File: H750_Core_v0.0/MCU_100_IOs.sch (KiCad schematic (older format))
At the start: 32 parts, among them U1 750VB_3Parts, U2 RESET, U3 USER, Y1 NX2016SA 25MHz, Y2 NX3215SA 32.768KHz

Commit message: PCB layout finished
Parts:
- JP1, JP10, JP11, JP12, JP13, JP14, JP15, JP16, JP2, JP3, JP4, JP5, JP6, JP7, JP8, JP9: footprint Resistor_SMD:R_0603_1608Metric -> H750_Core:JP
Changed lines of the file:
@@
 F 0 "JP1" H 5650 5635 50  0000 C CNN
 F 1 "Jumper_2_Open" H 5650 5544 50  0000 C CNN
-F 2 "Resistor_SMD:R_0603_1608Metric" H 5650 5400 50  0001 C CNN
+F 2 "H750_Core:JP" H 5650 5400 50  0001 C CNN
 F 3 "~" H 5650 5400 50  0001 C CNN
 	1    5650 5400
@@
 F 0 "JP2" H 5650 5735 50  0000 C CNN
 F 1 "Jumper_2_Open" H 5650 5644 50  0000 C CNN
-F 2 "Resistor_SMD:R_0603_1608Metric" H 5650 5500 50  0001 C CNN
+F 2 "H750_Core:JP" H 5650 5500 50  0001 C CNN
 F 3 "~" H 5650 5500 50  0001 C CNN
 	1    5650 5500
@@
 F 0 "JP10" H 5850 4495 50  0000 C CNN
 F 1 "Jumper_2_Bridged" H 5850 4404 50  0000 C CNN
-F 2 "Resistor_SMD:R_0603_1608Metric" H 5850 4300 50  0001 C CNN
+F 2 "H750_Core:JP" H 5850 4300 50  0001 C CNN
 F 3 "~" H 5850 4300 50  0001 C CNN
 	1    5850 4300
@@
 F 0 "JP9" H 5850 4195 50  0000 C CNN
 F 1 "Jumper_2_Bridged" H 5850 4104 50  0000 C CNN
-F 2 "Resistor_SMD:R_0603_1608Metric" H 5850 4000 50  0001 C CNN
+F 2 "H750_Core:JP" H 5850 4000 50  0001 C CNN
 F 3 "~" H 5850 4000 50  0001 C CNN
 	1    5850 4000
@@
 F 0 "JP4" H 5850 2595 50  0000 C CNN
 F 1 "Jumper_2_Bridged" H 5850 2504 50  0000 C CNN
-F 2 "Resistor_SMD:R_0603_1608Metric" H 5850 2400 50  0001 C CNN
+F 2 "H750_Core:JP" H 5850 2400 50  0001 C CNN
 F 3 "~" H 5850 2400 50  0001 C CNN
 	1    5850 2400
@@
 F 0 "JP3" H 5850 2495 50  0000 C CNN
 F 1 "Jumper_2_Bridged" H 5850 2404 50  0000 C CNN
-F 2 "Resistor_SMD:R_0603_1608Metric" H 5850 2300 50  0001 C CNN
+F 2 "H750_Core:JP" H 5850 2300 50  0001 C CNN
 F 3 "~" H 5850 2300 50  0001 C CNN
 	1    5850 2300
@@
 F 0 "JP5" H 5850 3095 50  0000 C CNN
 F 1 "Jumper_2_Bridged" H 5850 3004 50  0000 C CNN
-F 2 "Resistor_SMD:R_0603_1608Metric" H 5850 2900 50  0001 C CNN
+F 2 "H750_Core:JP" H 5850 2900 50  0001 C CNN
 F 3 "~" H 5850 2900 50  0001 C CNN
 	1    5850 2900
@@
 F 0 "JP11" H 5850 4595 50  0000 C CNN
 F 1 "Jumper_2_Bridged" H 5850 4504 50  0000 C CNN
-F 2 "Resistor_SMD:R_0603_1608Metric" H 5850 4400 50  0001 C CNN
+F 2 "H750_Core:JP" H 5850 4400 50  0001 C CNN
 F 3 "~" H 5850 4400 50  0001 C CNN
 	1    5850 4400
@@
 F 0 "JP14" H 9700 3595 50  0000 C CNN
 F 1 "Jumper_2_Bridged" H 9700 3504 50  0000 C CNN
-F 2 "Resistor_SMD:R_0603_1608Metric" H 9700 3400 50  0001 C CNN
+F 2 "H750_Core:JP" H 9700 3400 50  0001 C CNN
 F 3 "~" H 9700 3400 50  0001 C CNN
 	1    9700 3400
@@
 F 0 "JP13" H 9700 3495 50  0000 C CNN
 F 1 "Jumper_2_Bridged" H 9700 3404 50  0000 C CNN
-F 2 "Resistor_SMD:R_0603_1608Metric" H 9700 3300 50  0001 C CNN
+F 2 "H750_Core:JP" H 9700 3300 50  0001 C CNN
 F 3 "~" H 9700 3300 50  0001 C CNN
 	1    9700 3300
@@
 F 0 "JP15" H 9700 3695 50  0000 C CNN
 F 1 "Jumper_2_Bridged" H 9700 3604 50  0000 C CNN
-F 2 "Resistor_SMD:R_0603_1608Metric" H 9700 3500 50  0001 C CNN
+F 2 "H750_Core:JP" H 9700 3500 50  0001 C CNN
 F 3 "~" H 9700 3500 50  0001 C CNN
 	1    9700 3500
@@
 F 0 "JP12" H 9700 2695 50  0000 C CNN
 F 1 "Jumper_2_Bridged" H 9700 2604 50  0000 C CNN
-F 2 "Resistor_SMD:R_0603_1608Metric" H 9700 2500 50  0001 C CNN
+F 2 "H750_Core:JP" H 9700 2500 50  0001 C CNN
 F 3 "~" H 9700 2500 50  0001 C CNN
 	1    9700 2500
@@
 F 0 "JP8" H 5850 3895 50  0000 C CNN
 F 1 "Jumper_2_Bridged" H 5850 3804 50  0000 C CNN
-F 2 "Resistor_SMD:R_0603_1608Metric" H 5850 3700 50  0001 C CNN
+F 2 "H750_Core:JP" H 5850 3700 50  0001 C CNN
 F 3 "~" H 5850 3700 50  0001 C CNN
 	1    5850 3700
@@
 F 0 "JP7" H 5850 3795 50  0000 C CNN
 F 1 "Jumper_2_Bridged" H 5850 3704 50  0000 C CNN
-F 2 "Resistor_SMD:R_0603_1608Metric" H 5850 3600 50  0001 C CNN
+F 2 "H750_Core:JP" H 5850 3600 50  0001 C CNN
 F 3 "~" H 5850 3600 50  0001 C CNN
 	1    5850 3600
@@
 F 0 "JP6" H 5850 3695 50  0000 C CNN
 F 1 "Jumper_2_Bridged" H 5850 3604 50  0000 C CNN
-F 2 "Resistor_SMD:R_0603_1608Metric" H 5850 3500 50  0001 C CNN
+F 2 "H750_Core:JP" H 5850 3500 50  0001 C CNN
 F 3 "~" H 5850 3500 50  0001 C CNN
 	1    5850 3500
@@
 F 0 "JP16" H 13050 7745 50  0000 C CNN
 F 1 "Jumper_2_Bridged" H 13050 7654 50  0000 C CNN
-F 2 "Resistor_SMD:R_0603_1608Metric" H 13050 7550 50  0001 C CNN
+F 2 "H750_Core:JP" H 13050 7550 50  0001 C CNN
 F 3 "~" H 13050 7550 50  0001 C CNN
 	1    13050 7550

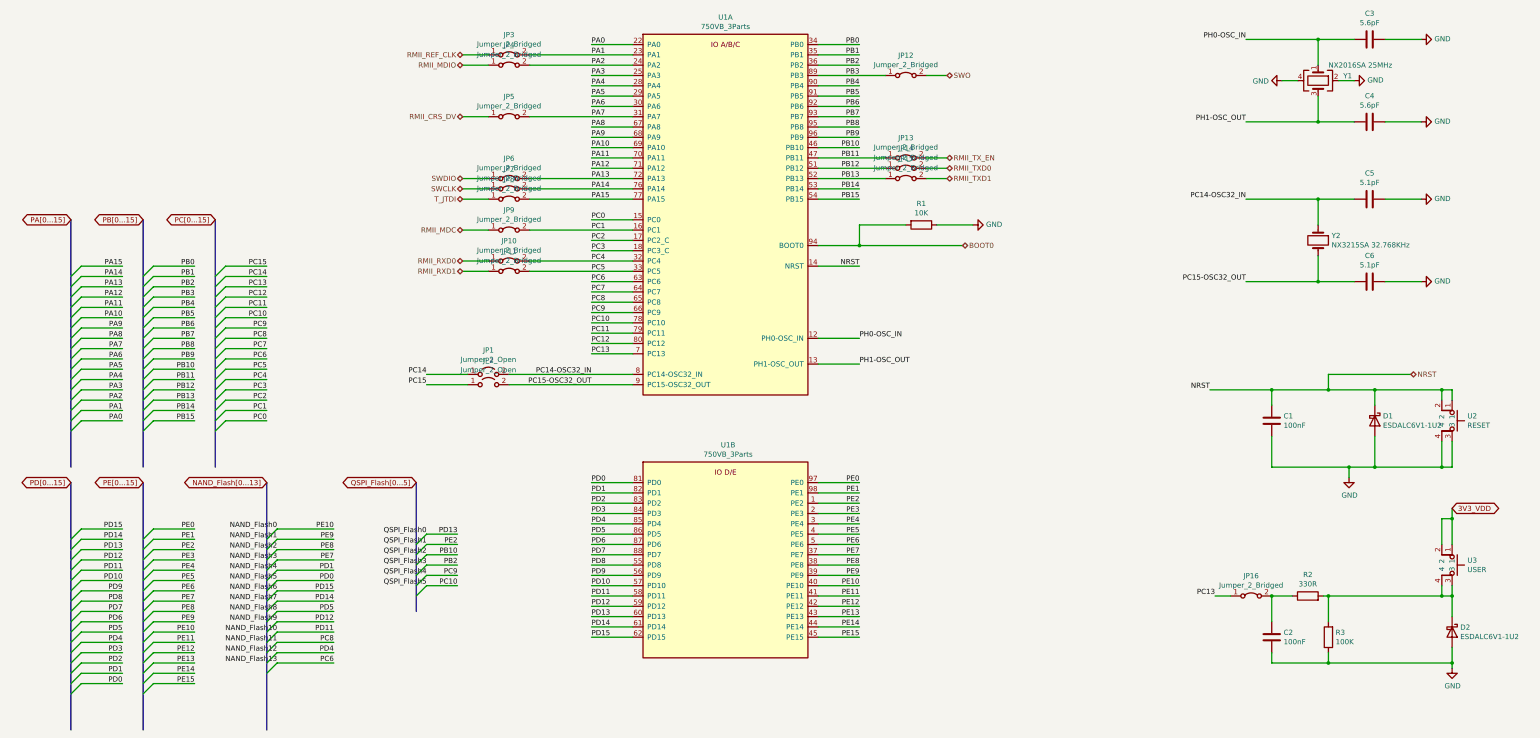
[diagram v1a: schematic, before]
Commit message: 修改编程接口
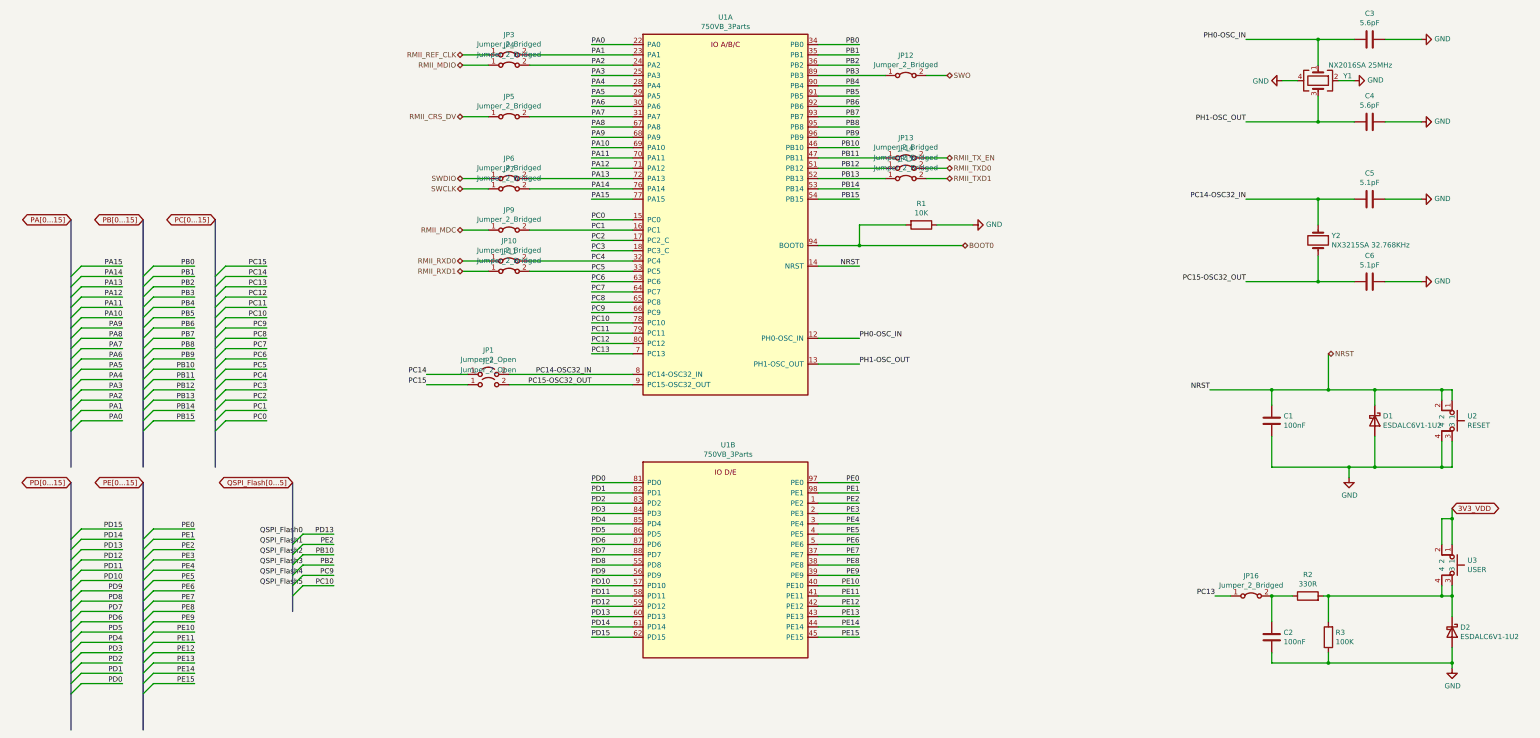
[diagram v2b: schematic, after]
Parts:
- removed JP8: Jumper_2_Bridged, H750_Core:JP, symbol Jumper:Jumper_2_Bridged
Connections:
- net NAND_Flash0 renamed PE10
- net NAND_Flash1 renamed PE9
- net NAND_Flash10 renamed PD11
- net NAND_Flash11 renamed PC8
- net NAND_Flash12 renamed PD4
- net NAND_Flash13 renamed PC6
- net NAND_Flash2 renamed PE8
- net NAND_Flash3 renamed PE7
- net NAND_Flash4 renamed PD1
- net NAND_Flash5 renamed PD0
- net NAND_Flash6 renamed PD15
- net NAND_Flash7 renamed PD14
- net NAND_Flash8 renamed PD5
- net NAND_Flash9 renamed PD12
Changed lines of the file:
@@
 EESchema Schematic File Version 4
-LIBS:H750_Core-cache
 EELAYER 30 0
 EELAYER END
@@
 Text HLabel 5400 3600 0    50   BiDi ~ 0
 SWCLK
-Text HLabel 5400 3700 0    50   BiDi ~ 0
-T_JTDI
 $Comp
 L Jumper:Jumper_2_Bridged JP12
@@
 	1    0    0    -1
 $EndComp
-$Comp
-L Jumper:Jumper_2_Bridged JP8
-U 1 1 5DA28DD9
-P 5850 3700
-F 0 "JP8" H 5850 3895 50  0000 C CNN
-F 1 "Jumper_2_Bridged" H 5850 3804 50  0000 C CNN
-F 2 "H750_Core:JP" H 5850 3700 50  0001 C CNN
-F 3 "~" H 5850 3700 50  0001 C CNN
-	1    5850 3700
-	1    0    0    -1
-$EndComp
-Wire Wire Line
-	6050 3700 7050 3700
-Wire Wire Line
-	5650 3700 5400 3700
 $Comp
 L Jumper:Jumper_2_Bridged JP7
@@
 Wire Wire Line
 	14900 6300 14250 6300
-Text HLabel 14600 5400 2    50   BiDi ~ 0
-NRST
 Wire Wire Line
 	15000 5650 15000 5550
@@
 Wire Wire Line
 	14250 5550 14250 5700
-Wire Wire Line
-	14250 5550 13800 5550
 Wire Wire Line
 	13250 5550 13250 5700
 Connection ~ 14250 5550
-Wire Wire Line
-	14600 5400 13800 5400
-Wire Wire Line
-	13800 5400 13800 5550
-Connection ~ 13800 5550
-Wire Wire Line
-	13800 5550 13250 5550
 Text Label 12650 5550 2    50   ~ 0
 NRST
@@
 Connection ~ 14900 7550
 Connection ~ 13800 7550
-Entry Wire Line
-	3500 8300 3600 8200
-Entry Wire Line
-	3500 8200 3600 8100
-Entry Wire Line
-	3500 8100 3600 8000
-Entry Wire Line
-	3500 8000 3600 7900
-Entry Wire Line
-	3500 7900 3600 7800
-Entry Wire Line
-	3500 7800 3600 7700
-Entry Wire Line
-	3500 7700 3600 7600
-Entry Wire Line
-	3500 7600 3600 7500
-Entry Wire Line
-	3500 7500 3600 7400
-Entry Wire Line
-	3500 7400 3600 7300
-Entry Wire Line
-	3500 7300 3600 7200
-Entry Wire Line
-	3500 7200 3600 7100
-Entry Wire Line
-	3500 7100 3600 7000
-Entry Wire Line
-	3500 7000 3600 6900
-Text Label 4150 8200 2    50   ~ 0
-PC6
-Text Label 4150 8100 2    50   ~ 0
-PD4
-Text Label 4150 8000 2    50   ~ 0
-PC8
-Text Label 4150 7900 2    50   ~ 0
-PD11
-Text Label 4150 7800 2    50   ~ 0
-PD12
-Text Label 4150 7700 2    50   ~ 0
-PD5
-Text Label 4150 7600 2    50   ~ 0
-PD14
-Text Label 4150 7500 2    50   ~ 0
-PD15
-Text Label 4150 7400 2    50   ~ 0
-PD0
-Text Label 4150 7300 2    50   ~ 0
-PD1
-Text Label 4150 7200 2    50   ~ 0
-PE7
-Text Label 4150 7100 2    50   ~ 0
-PE8
-Text Label 4150 7000 2    50   ~ 0
-PE9
-Text Label 4150 6900 2    50   ~ 0
-PE10
 Text GLabel 1600 3900 0    50   BiDi ~ 0
 PA[0...15]
@@
 Text GLabel 2300 6450 0    50   BiDi ~ 0
 PE[0...15]
-Text GLabel 3500 6450 0    50   BiDi ~ 0
-NAND_Flash[0...13]
 Wire Wire Line
 	14900 5650 14900 5550
@@
 	0    1    1    0
 $EndComp
-Text Label 3600 6900 2    50   ~ 0
-NAND_Flash0
-Text Label 3600 7000 2    50   ~ 0
-NAND_Flash1
-Text Label 3600 7100 2    50   ~ 0
-NAND_Flash2
-Text Label 3600 7200 2    50   ~ 0
-NAND_Flash3
-Text Label 3600 7300 2    50   ~ 0
-NAND_Flash4
-Text Label 3600 7400 2    50   ~ 0
-NAND_Flash5
-Text Label 3600 7700 2    50   ~ 0
-NAND_Flash8
-Text Label 3600 7500 2    50   ~ 0
-NAND_Flash6
-Text Label 3600 7600 2    50   ~ 0
-NAND_Flash7
-Wire Wire Line
-	3600 6900 4150 6900
-Text Label 3600 7800 2    50   ~ 0
-NAND_Flash9
-Text Label 3600 7900 2    50   ~ 0
-NAND_Flash10
-Text Label 3600 8000 2    50   ~ 0
-NAND_Flash11
-Text Label 3600 8100 2    50   ~ 0
-NAND_Flash12
-Text Label 3600 8200 2    50   ~ 0
-NAND_Flash13
-Wire Wire Line
-	3600 8200 4150 8200
-Wire Wire Line
-	3600 8100 4150 8100
-Wire Wire Line
-	3600 8000 4150 8000
-Wire Wire Line
-	3600 7900 4150 7900
-Wire Wire Line
-	3600 7800 4150 7800
-Wire Wire Line
-	3600 7700 4150 7700
-Wire Wire Line
-	3600 7600 4150 7600
-Wire Wire Line
-	3600 7500 4150 7500
-Wire Wire Line
-	3600 7400 4150 7400
-Wire Wire Line
-	3600 7300 4150 7300
-Wire Wire Line
-	3600 7200 4150 7200
-Wire Wire Line
-	3600 7100 4150 7100
-Wire Wire Line
-	3600 7000 4150 7000
-Wire Wire Line
-	5050 7450 5350 7450
-Text Label 5350 7450 2    50   ~ 0
+Wire Wire Line
+	3850 7450 4150 7450
+Text Label 4150 7450 2    50   ~ 0
 PC10
 Wire Wire Line
-	5050 7350 5350 7350
-Text Label 5350 7350 2    50   ~ 0
+	3850 7350 4150 7350
+Text Label 4150 7350 2    50   ~ 0
 PC9
 Wire Wire Line
-	5050 7250 5350 7250
-Text Label 5350 7250 2    50   ~ 0
+	3850 7250 4150 7250
+Text Label 4150 7250 2    50   ~ 0
 PB2
 Wire Wire Line
-	5050 7150 5350 7150
-Text Label 5350 7150 2    50   ~ 0
+	3850 7150 4150 7150
+Text Label 4150 7150 2    50   ~ 0
 PB10
 Wire Wire Line
-	5050 7050 5350 7050
-Text Label 5350 7050 2    50   ~ 0
+	3850 7050 4150 7050
+Text Label 4150 7050 2    50   ~ 0
 PE2
 Wire Wire Line
-	5050 6950 5350 6950
-Text Label 5350 6950 2    50   ~ 0
+	3850 6950 4150 6950
+Text Label 4150 6950 2    50   ~ 0
 PD13
 Entry Wire Line
-	4950 7450 5050 7350
-Entry Wire Line
-	4950 7350 5050 7250
-Entry Wire Line
-	4950 7250 5050 7150
-Entry Wire Line
-	4950 7150 5050 7050
-Entry Wire Line
-	4950 7050 5050 6950
-Text GLabel 4950 6450 0    50   BiDi ~ 0
+	3750 7450 3850 7350
+Entry Wire Line
+	3750 7350 3850 7250
+Entry Wire Line
+	3750 7250 3850 7150
+Entry Wire Line
+	3750 7150 3850 7050
+Entry Wire Line
+	3750 7050 3850 6950
+Text GLabel 3750 6450 0    50   BiDi ~ 0
 QSPI_Flash[0...5]
-Text Label 5050 6950 2    50   ~ 0
+Text Label 3850 6950 2    50   ~ 0
 QSPI_Flash0
-Text Label 5050 7050 2    50   ~ 0
+Text Label 3850 7050 2    50   ~ 0
 QSPI_Flash1
-Text Label 5050 7150 2    50   ~ 0
+Text Label 3850 7150 2    50   ~ 0
 QSPI_Flash2
-Text Label 5050 7250 2    50   ~ 0
+Text Label 3850 7250 2    50   ~ 0
 QSPI_Flash3
-Text Label 5050 7350 2    50   ~ 0
+Text Label 3850 7350 2    50   ~ 0
 QSPI_Flash4
-Text Label 5050 7450 2    50   ~ 0
+Text Label 3850 7450 2    50   ~ 0
 QSPI_Flash5
 Entry Wire Line
-	4950 7550 5050 7450
+	3750 7550 3850 7450
+Wire Wire Line
+	13250 5550 13800 5550
+Wire Wire Line
+	6650 3700 7050 3700
+Text HLabel 13800 5200 2    50   BiDi ~ 0
+NRST
+Wire Wire Line
+	13800 5200 13800 5550
+Connection ~ 13800 5550
+Wire Wire Line
+	13800 5550 14250 5550
 Wire Bus Line
-	4950 6450 4950 7700
-Wire Bus Line
-	3500 6450 3500 8850
+	3750 6450 3750 7700
 Wire Bus Line
 	1600 3900 1600 6300
